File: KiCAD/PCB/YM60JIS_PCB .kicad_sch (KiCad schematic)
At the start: 165 parts, among them J1 TYPE-C-31-M-12, SW1 SW_Push, SW10 SW_Push, SW11 SW_Push, SW12 SW_Push, SW13 SW_Push, SW14 SW_Push, SW15 SW_Push, SW16 SW_Push, SW17 SW_Push, SW18 SW_Push, SW19 SW_Push, SW2 SW_Push, SW20 SW_Push, SW21 SW_Push, SW22 SW_Push, SW23 SW_Push, SW24 SW_Push, SW25 SW_Push, SW26 SW_Push, SW27 SW_Push, SW28 SW_Push, SW29 Space, SW3 SW_Push, SW30 SW_Push, SW31 SW_Push, SW32 SW_Push, SW33 SW_Push, SW34 SW_Push, SW35 SW_Push, SW36 SW_Push, SW37 SW_Push, SW38 SW_Push, SW39 SW_Push, SW4 SW_Push, SW40 SW_Push, SW41 SW_Push, SW42 SW_Push, SW43 SW_Push, SW44 SW_Push, SW45 SW_Push, SW46 SW_Push, SW47 SW_Push, SW48 SW_Push, SW49 SW_Push, SW5 SW_Push, SW50 SW_Push, SW51 SW_Push, SW52 SW_Push, SW53 SW_Push, SW54 SW_Push, SW55 SW_Push, SW56 SW_Push, SW57 SW_Push, SW58 SW_Push, SW59 SW_Push, SW6 SW_Push, SW60 SW_Push, SW61 SW_Push, SW62 SW_Push, SW63 Yen, SW64 Backspace, SW65 ISOEnter, SW66 SW_Push, SW67 SW_Push, SW7 SW_Push, SW8 SW_Push, SW9 SW_Push, U1 XC6206P332MR, U2 SMF05CT1G, U3 RP2040, U4 W25Q16JVUXIQ, Y1 X322512MSB4SI

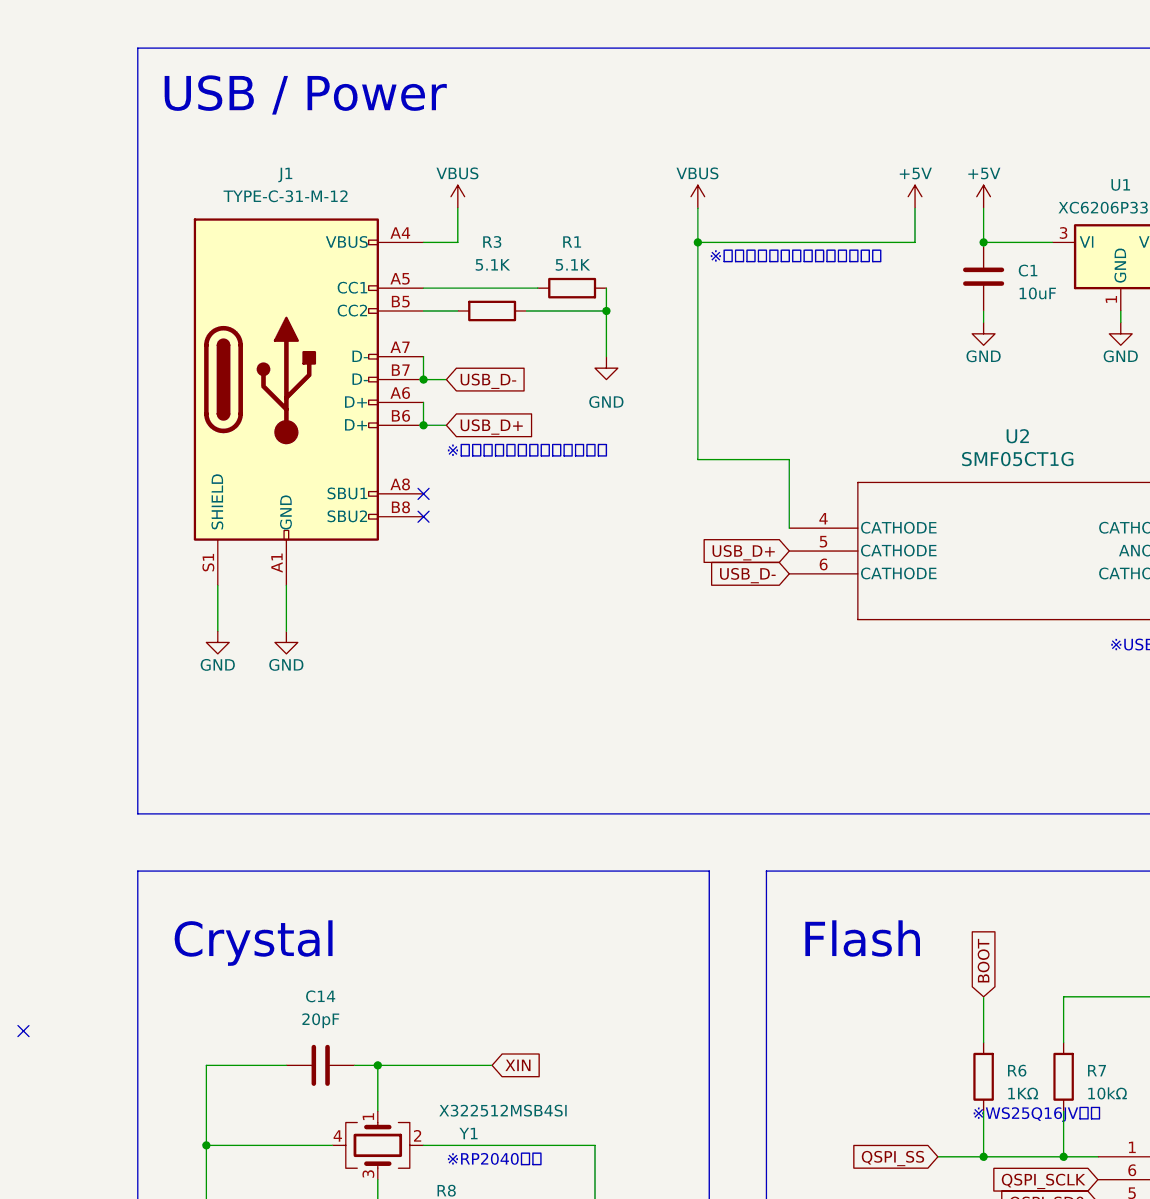
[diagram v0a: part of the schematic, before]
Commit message: PCBの設計データリネームとフォルダ移動
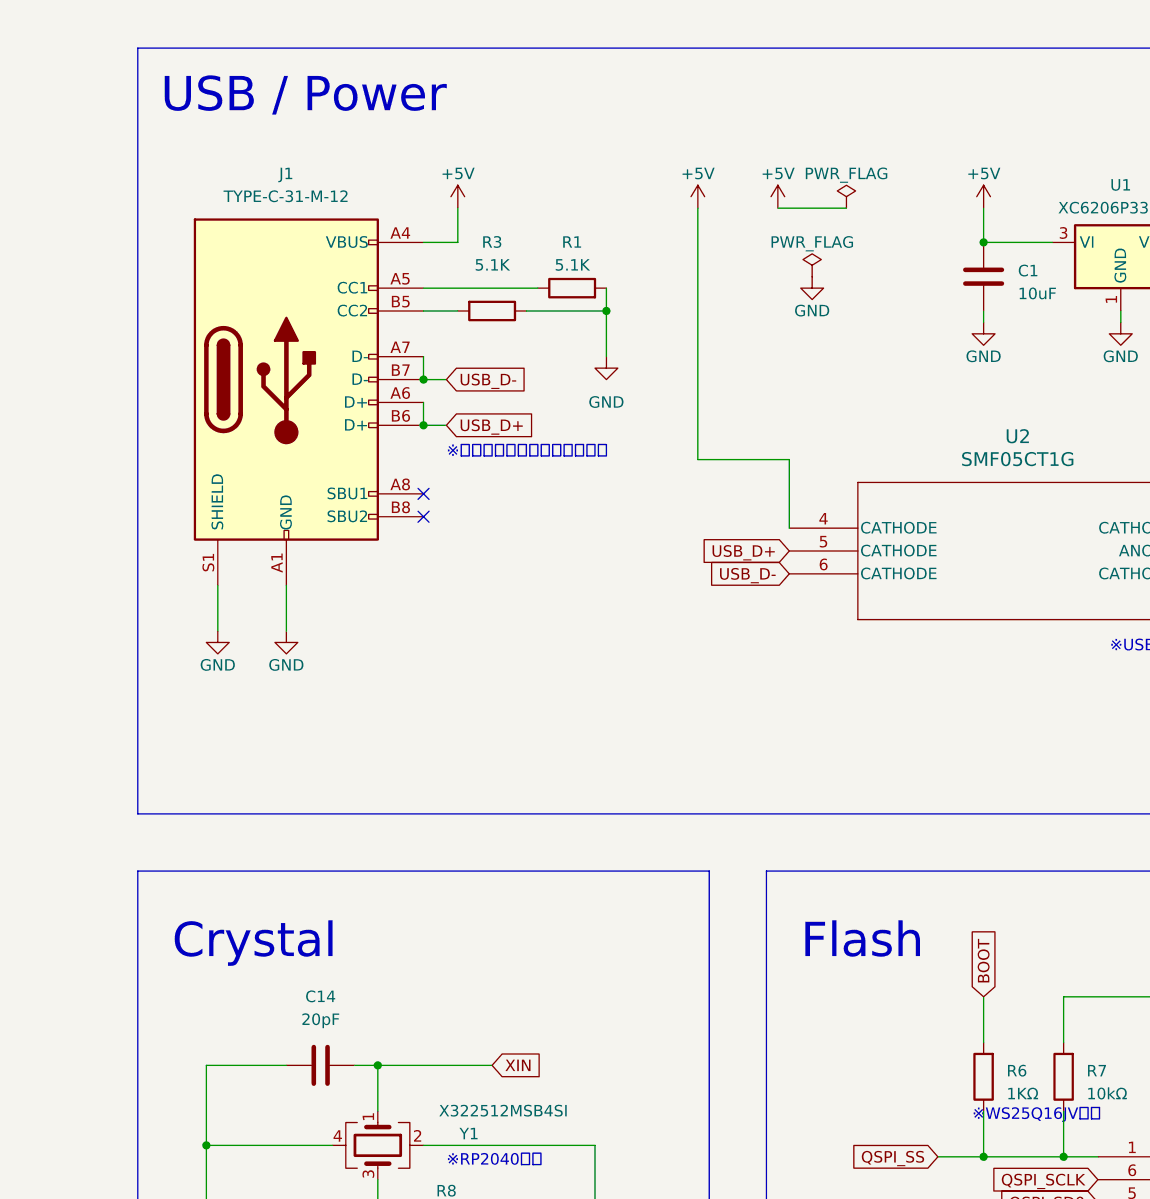
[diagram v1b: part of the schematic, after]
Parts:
- U4: JLCPCB Rotation Offset 180 -> 90
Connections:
- no-connect marks 16 -> 15
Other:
- note removed: "※以前はここにヒューズがあった"
- title: YM60JIS -> YM60JIS PCB

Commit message: ライブラリの参照先をsubmodulesに変更
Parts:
- J1: symbol Connector:USB_C_Receptacle_USB2.0 -> Connector:USB_C_Receptacle_USB2.0_16P
- SW1, SW11, SW12, SW13, SW14, SW16, SW17, SW18, SW19, SW21, SW22, SW23, SW24, SW25, SW26, SW27, SW28, SW30, SW31, SW32, SW33, SW34, SW35, SW36, SW37, SW38, SW39, SW40, SW41, SW43, SW44, SW45, SW46, SW48, SW49, SW50, SW51, SW53, SW54, SW55, SW56, SW57, SW58, SW59, SW6, SW60, SW61, SW62, SW63, SW64, SW66, SW67, SW7, SW8, SW9: footprint Switch_Keyboard_Hotswap_Kailh:SW_Hotswap_Kailh_MX_1.00u -> PCM_Switch_Keyboard_Hotswap_Kailh:SW_Hotswap_Kailh_MX_1.00u
- SW10, SW15, SW20, SW42, SW47, SW52: footprint Switch_Keyboard_Hotswap_Kailh:SW_Hotswap_Kailh_MX_1.25u -> PCM_Switch_Keyboard_Hotswap_Kailh:SW_Hotswap_Kailh_MX_1.25u
- SW2, SW5: footprint Switch_Keyboard_Hotswap_Kailh:SW_Hotswap_Kailh_MX_1.50u -> PCM_Switch_Keyboard_Hotswap_Kailh:SW_Hotswap_Kailh_MX_1.50u
- SW29: footprint Switch_Keyboard_Hotswap_Kailh:SW_Hotswap_Kailh_MX_3.00u -> PCM_Switch_Keyboard_Hotswap_Kailh:SW_Hotswap_Kailh_MX_3.00u
- SW3: footprint Switch_Keyboard_Hotswap_Kailh:SW_Hotswap_Kailh_MX_1.75u -> PCM_Switch_Keyboard_Hotswap_Kailh:SW_Hotswap_Kailh_MX_1.75u
- SW4: footprint Switch_Keyboard_Hotswap_Kailh:SW_Hotswap_Kailh_MX_2.00u -> PCM_Switch_Keyboard_Hotswap_Kailh:SW_Hotswap_Kailh_MX_2.00u
- SW65: footprint Switch_Keyboard_Hotswap_Kailh:SW_Hotswap_Kailh_MX_ISOEnter -> PCM_Switch_Keyboard_Hotswap_Kailh:SW_Hotswap_Kailh_MX_ISOEnter
